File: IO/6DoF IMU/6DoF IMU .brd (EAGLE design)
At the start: 25.4 x 25.4 mm, 3 parts

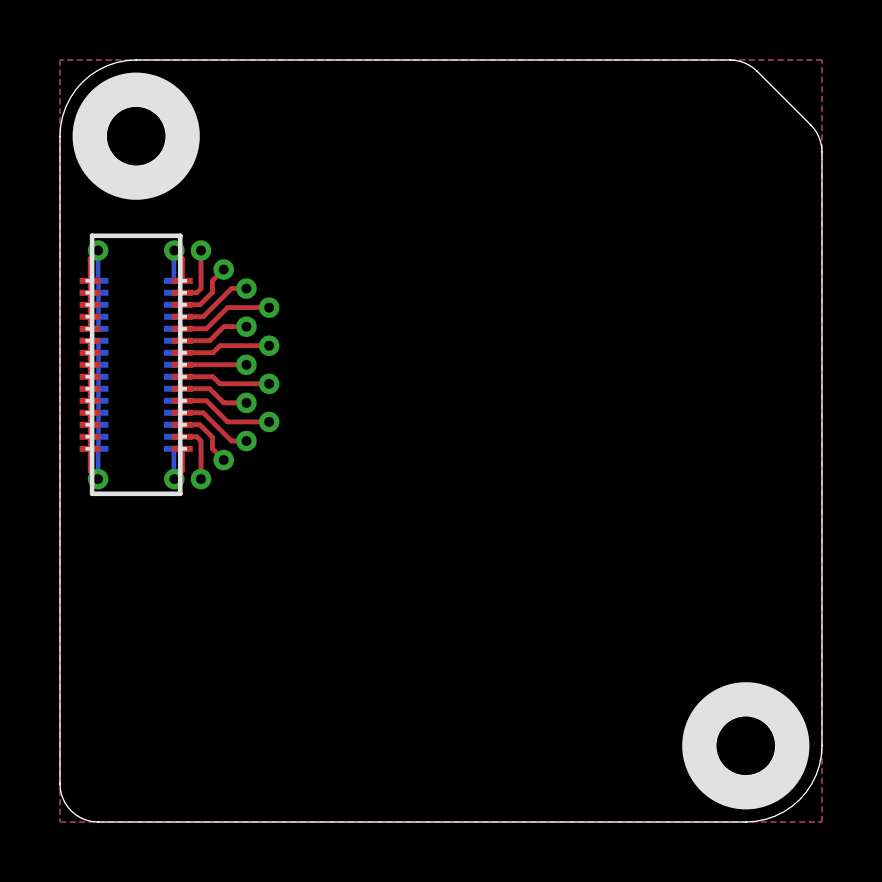
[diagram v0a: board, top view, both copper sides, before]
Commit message: Updated concepts/ideas Renamed 6DoF IMU files Created 6DoF IMU sch and brd  (Missing 8-1 smd jumper)
Signed-off-by: Cruz Monrreal II <Cruz.Monrreal@gmail.com>
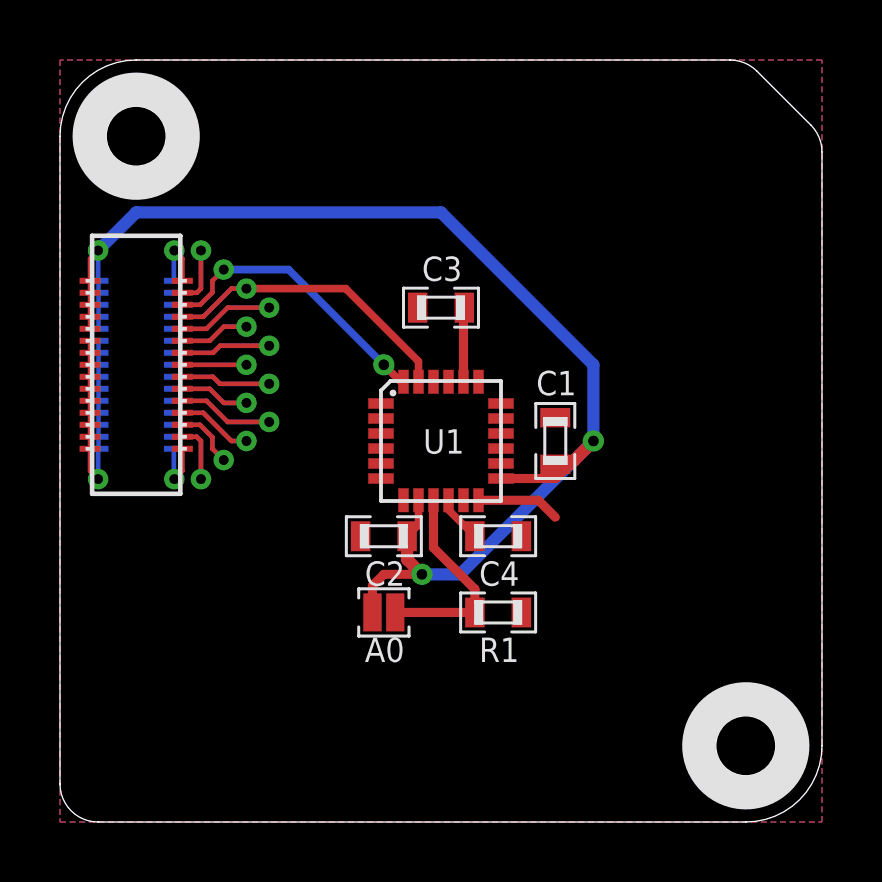
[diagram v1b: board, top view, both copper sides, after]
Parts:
- added A0: (no value), .solderjumper:2.LRG
- added C1, C4: .1uF, .standardparts:0603
- added C2, C3: 10nF, .standardparts:0603
- added R1: (no value), .standardparts:0603
- added U1: MPU-6050, invensense:QFN
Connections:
- removed net N$10: U$8.03, U$8.03@1, U$8.03@VIA
- removed net N$11: U$8.04, U$8.04@1, U$8.04@VIA
- removed net N$12: U$8.05, U$8.05@1, U$8.05@VIA
- removed net N$13: U$8.06, U$8.06@1, U$8.06@VIA
- removed net N$14: U$8.07, U$8.07@1, U$8.07@VIA
- removed net N$15: U$8.WAKE, U$8.WAKE@1, U$8.WAKE@VIA
- removed net N$3: U$8.SDA, U$8.SDA@1, U$8.SDA@VIA
- removed net N$4: U$8.SCL, U$8.SCL@1, U$8.SCL@VIA
- removed net N$8: U$8.01, U$8.01@1, U$8.01@VIA
- removed net N$9: U$8.02, U$8.02@1, U$8.02@VIA
- new net INT: U1.12
- new net N$16: C3.2, U1.20
- new net N$18: A0.2, R1.1, U1.9
- new net N$20: C4.2, U1.10
- new net SCL: U$8.SCL, U$8.SCL@1, U$8.SCL@VIA, U1.23
- new net SDA: U$8.SDA, U$8.SDA@1, U$8.SDA@VIA, U1.24
- net 3.3V: now also A0.1, C1.2, C2.1, U1.13, U1.8
- net GND: now also C1.1, C2.2, C3.1, C4.1, R1.2, U1.1, U1.18
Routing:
- net 3.3V: track 0.00 -> 39.1 mm, vias 0 -> 2
- net SDA: track 0.00 -> 7.67 mm, vias 0 -> 1
- net SCL: track 0.00 -> 7.42 mm
- net N$18: track 0.00 -> 6.97 mm
- net INT: track 0.00 -> 2.79 mm
- net N$16: track 0.00 -> 2.48 mm
- net N$20: track 0.00 -> 1.56 mm
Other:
- board text added: "* Create 8-1 SMD Jumper"
- board text added: "6DoF IMU"
- board text added: "Addr: 110100"
- board text added: "Cruz Monrreal II"
- board text added: "InnovativeMaker.com"
- board text added: "MPU6050"
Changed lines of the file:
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@@
 <layer number="50" name="dxf" color="7" fill="1" visible="no" active="no"/>
 <layer number="51" name="tDocu" color="7" fill="1" visible="yes" active="yes"/>
-<layer number="52" name="bDocu" color="7" fill="1" visible="no" active="yes"/>
+<layer number="52" name="bDocu" color="7" fill="1" visible="yes" active="yes"/>
 <layer number="53" name="tGND_GNDA" color="7" fill="9" visible="no" active="no"/>
 <layer number="54" name="bGND_GNDA" color="1" fill="9" visible="no" active="no"/>
@@
 <wire x1="22.33395" y1="25.4" x2="2.54" y2="25.4" width="0" layer="20"/>
 <wire x1="2.54" y1="25.4" x2="0" y2="22.86" width="0" layer="20" curve="90"/>
+<text x="13.97" y="23.495" size="1.27" layer="51" ratio="12">MPU6050</text>
+<text x="13.97" y="22.225" size="1.016" layer="51" ratio="12">6DoF IMU</text>
+<text x="13.97" y="20.955" size="1.016" layer="51" ratio="12">Addr: 110100</text>
+<text x="12.065" y="1.905" size="0.8128" layer="52" ratio="12" rot="MR0" align="bottom-center">Cruz Monrreal II</text>
+<text x="12.065" y="0.635" size="0.8128" layer="52" ratio="12" rot="MR0" align="bottom-center">InnovativeMaker.com</text>
+<text x="27.305" y="13.335" size="0.8128" layer="51" ratio="12" rot="R90" align="bottom-center">* Create 8-1 SMD Jumper</text>
 </plain>
 <attributes>
@@
 <element name="U$3" library=".screw_holes" package="2MM" value="HOLE.2MM" x="22.86" y="2.54" rot="R90"/>
 <element name="U$8" library="thinkmaketest" package="ROOT1.BOTH" value="ROOT1.BOTH" x="0" y="0"/>
+<element name="U1" library="invensense" package="QFN" value="MPU-6050" x="12.7" y="12.7" smashed="yes">
+<attribute name="NAME" x="12.105" y="12.279" size="0.8128" layer="25" font="vector" ratio="12"/>
+</element>
+<element name="C1" library=".standardparts" package="0603" value=".1uF" x="16.51" y="12.7" smashed="yes" rot="R270">
+<attribute name="NAME" x="15.875" y="14.224" size="0.8128" layer="25" font="vector" ratio="12"/>
+</element>
+<element name="C2" library=".standardparts" package="0603" value="10nF" x="10.795" y="9.525" smashed="yes" rot="R180">
+<attribute name="NAME" x="10.16" y="7.874" size="0.8128" layer="25" font="vector" ratio="12"/>
+</element>
+<element name="C3" library=".standardparts" package="0603" value="10nF" x="12.7" y="17.145" smashed="yes">
+<attribute name="NAME" x="12.065" y="18.034" size="0.8128" layer="25" font="vector" ratio="12"/>
+</element>
+<element name="C4" library=".standardparts" package="0603" value=".1uF" x="14.605" y="9.525" smashed="yes" rot="R180">
+<attribute name="NAME" x="13.97" y="7.874" size="0.8128" layer="25" font="vector" ratio="12"/>
+</element>
+<element name="A0" library=".solderjumper" package="2.LRG" value="" x="10.795" y="6.985" smashed="yes">
+<attribute name="NAME" x="10.16" y="5.334" size="0.8128" layer="25" ratio="12"/>
+<attribute name="VALUE" x="9.795" y="5.485" size="0.4064" layer="27"/>
+</element>
+<element name="R1" library=".standardparts" package="0603" value="" x="14.605" y="6.985" smashed="yes">
+<attribute name="NAME" x="13.97" y="5.334" size="0.8128" layer="25" font="vector" ratio="12"/>
+<attribute name="VALUE" x="13.335" y="5.715" size="0.4064" layer="27" font="vector"/>
+</element>
 </elements>
 <signals>
@@
 <contactref element="U$8" pad="GND@15"/>
 <contactref element="U$8" pad="GND@VIA"/>
-</signal>
-<signal name="N$18">
+<contactref element="U1" pad="18"/>
+<contactref element="C3" pad="1"/>
+<contactref element="U1" pad="1"/>
+<contactref element="C1" pad="1"/>
+<contactref element="C2" pad="2"/>
+<contactref element="C4" pad="1"/>
+<contactref element="R1" pad="2"/>
 </signal>
 <signal name="N$20">
-</signal>
-<signal name="N$21">
-</signal>
-<signal name="N$22">
+<contactref element="C4" pad="2"/>
+<contactref element="U1" pad="10"/>
+<wire x1="12.95" y1="10.725" x2="12.95" y2="10.405" width="0.254" layer="1"/>
+<wire x1="12.95" y1="10.405" x2="13.83" y2="9.525" width="0.254" layer="1"/>
+</signal>
+<signal name="SDA">
+<contactref element="U1" pad="24"/>
+<contactref element="U$8" pad="SDA"/>
+<contactref element="U$8" pad="SDA@1"/>
+<contactref element="U$8" pad="SDA@VIA"/>
+<wire x1="11.45" y1="14.675" x2="11.45" y2="14.585" width="0.254" layer="1"/>
+<wire x1="11.45" y1="14.585" x2="10.795" y2="15.24" width="0.254" layer="1"/>
+<via x="10.795" y="15.24" extent="1-16" drill="0.3556"/>
+<wire x1="10.795" y1="15.24" x2="7.62" y2="18.415" width="0.254" layer="16"/>
+<wire x1="7.62" y1="18.415" x2="5.457" y2="18.415" width="0.254" layer="16"/>
+</signal>
+<signal name="SCL">
+<contactref element="U1" pad="23"/>
+<contactref element="U$8" pad="SCL"/>
+<contactref element="U$8" pad="SCL@1"/>
+<contactref element="U$8" pad="SCL@VIA"/>
+<wire x1="11.95" y1="14.675" x2="11.95" y2="15.355" width="0.254" layer="1"/>
+<wire x1="11.95" y1="15.355" x2="9.525" y2="17.78" width="0.254" layer="1"/>
+<wire x1="9.525" y1="17.78" x2="6.215" y2="17.78" width="0.254" layer="1"/>
 </signal>
 <signal name="N$24">
@@
 <contactref element="U$8" pad="3.3V@8"/>
 <contactref element="U$8" pad="3.3V@VIA"/>
+<contactref element="U1" pad="8"/>
+<contactref element="U1" pad="13"/>
+<contactref element="C1" pad="2"/>
+<contactref element="C2" pad="1"/>
+<contactref element="A0" pad="1"/>
+<wire x1="1.27" y1="19.05" x2="2.54" y2="20.32" width="0.4064" layer="16"/>
+<wire x1="2.54" y1="20.32" x2="12.7" y2="20.32" width="0.4064" layer="16"/>
+<wire x1="12.7" y1="20.32" x2="17.78" y2="15.24" width="0.4064" layer="16"/>
+<wire x1="17.78" y1="15.24" x2="17.78" y2="12.7" width="0.4064" layer="16"/>
+<wire x1="11.95" y1="10.725" x2="11.95" y2="9.905" width="0.254" layer="1"/>
+<wire x1="11.95" y1="9.905" x2="11.57" y2="9.525" width="0.254" layer="1"/>
+<via x="12.065" y="8.255" extent="1-16" drill="0.3556"/>
+<wire x1="17.78" y1="12.7" x2="13.335" y2="8.255" width="0.4064" layer="16"/>
+<wire x1="13.335" y1="8.255" x2="12.065" y2="8.255" width="0.4064" layer="16"/>
+<wire x1="12.065" y1="8.255" x2="11.57" y2="8.75" width="0.4064" layer="1"/>
+<wire x1="11.57" y1="8.75" x2="11.57" y2="9.525" width="0.4064" layer="1"/>
+<wire x1="16.51" y1="11.925" x2="17.005" y2="11.925" width="0.4064" layer="1"/>
+<wire x1="17.005" y1="11.925" x2="17.145" y2="12.065" width="0.4064" layer="1"/>
+<via x="17.78" y="12.7" extent="1-16" drill="0.3556"/>
+<wire x1="17.145" y1="12.065" x2="17.78" y2="12.7" width="0.4064" layer="1"/>
+<wire x1="14.7" y1="11.45" x2="16.53" y2="11.45" width="0.3048" layer="1"/>
+<wire x1="16.53" y1="11.45" x2="17.145" y2="12.065" width="0.3048" layer="1"/>
+<wire x1="12.065" y1="8.255" x2="10.795" y2="8.255" width="0.3048" layer="1"/>
+<wire x1="10.795" y1="8.255" x2="10.414" y2="7.874" width="0.3048" layer="1"/>
+<wire x1="10.414" y1="7.874" x2="10.414" y2="6.985" width="0.3048" layer="1"/>
 </signal>
 <signal name="N$1">
@@
 <contactref element="U$8" pad="ADC1@VIA"/>
 </signal>
-<signal name="N$3">
-<contactref element="U$8" pad="SDA"/>
-<contactref element="U$8" pad="SDA@1"/>
-<contactref element="U$8" pad="SDA@VIA"/>
-</signal>
-<signal name="N$4">
-<contactref element="U$8" pad="SCL"/>
-<contactref element="U$8" pad="SCL@1"/>
-<contactref element="U$8" pad="SCL@VIA"/>
-</signal>
 <signal name="N$5">
 <contactref element="U$8" pad="MOSI@VIA"/>
@@
 <contactref element="U$8" pad="SCLK@VIA"/>
 </signal>
-<signal name="N$8">
-<contactref element="U$8" pad="01@VIA"/>
-<contactref element="U$8" pad="01@1"/>
-<contactref element="U$8" pad="01"/>
-</signal>
-<signal name="N$9">
-<contactref element="U$8" pad="02@VIA"/>
-<contactref element="U$8" pad="02@1"/>
-<contactref element="U$8" pad="02"/>
-</signal>
-<signal name="N$10">
-<contactref element="U$8" pad="03@1"/>
-<contactref element="U$8" pad="03@VIA"/>
-<contactref element="U$8" pad="03"/>
-</signal>
-<signal name="N$11">
-<contactref element="U$8" pad="04@VIA"/>
-<contactref element="U$8" pad="04@1"/>
-<contactref element="U$8" pad="04"/>
-</signal>
-<signal name="N$12">
-<contactref element="U$8" pad="05"/>
-<contactref element="U$8" pad="05@VIA"/>
-<contactref element="U$8" pad="05@1"/>
-</signal>
-<signal name="N$13">
-<contactref element="U$8" pad="06"/>
-<contactref element="U$8" pad="06@VIA"/>
-<contactref element="U$8" pad="06@1"/>
-</signal>
-<signal name="N$14">
-<contactref element="U$8" pad="07@VIA"/>
-<contactref element="U$8" pad="07@1"/>
-<contactref element="U$8" pad="07"/>
-</signal>
-<signal name="N$15">
-<contactref element="U$8" pad="WAKE@VIA"/>
-<contactref element="U$8" pad="WAKE@1"/>
-<contactref element="U$8" pad="WAKE"/>
+<signal name="N$16">
+<contactref element="U1" pad="20"/>
+<contactref element="C3" pad="2"/>
+<wire x1="13.45" y1="14.675" x2="13.45" y2="17.12" width="0.3048" layer="1"/>
+<wire x1="13.45" y1="17.12" x2="13.475" y2="17.145" width="0.3048" layer="1"/>
+</signal>
+<signal name="INT">
+<contactref element="U1" pad="12"/>
+<wire x1="13.95" y1="10.725" x2="15.945" y2="10.725" width="0.3048" layer="1"/>
+<wire x1="15.945" y1="10.725" x2="16.51" y2="10.16" width="0.3048" layer="1"/>
+</signal>
+<signal name="N$18">
+<contactref element="R1" pad="1"/>
+<contactref element="A0" pad="2"/>
+<contactref element="U1" pad="9"/>
+<wire x1="12.45" y1="10.725" x2="12.45" y2="9.14" width="0.3048" layer="1"/>
+<wire x1="12.45" y1="9.14" x2="13.83" y2="7.76" width="0.3048" layer="1"/>
+<wire x1="13.83" y1="7.76" x2="13.83" y2="6.985" width="0.3048" layer="1"/>
+<wire x1="11.176" y1="6.985" x2="13.83" y2="6.985" width="0.3048" layer="1"/>
 </signal>
 </signals>
